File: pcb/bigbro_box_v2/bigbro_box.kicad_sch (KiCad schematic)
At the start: 41 parts, among them J1 Current Sense, J2 Display, J3 Mains, J4 UART flashing, J5 RFID, J6 Relay, K1 G5LE-1, Q1 MMBT3904, Q2 MMBT3904, Q3 BSS138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

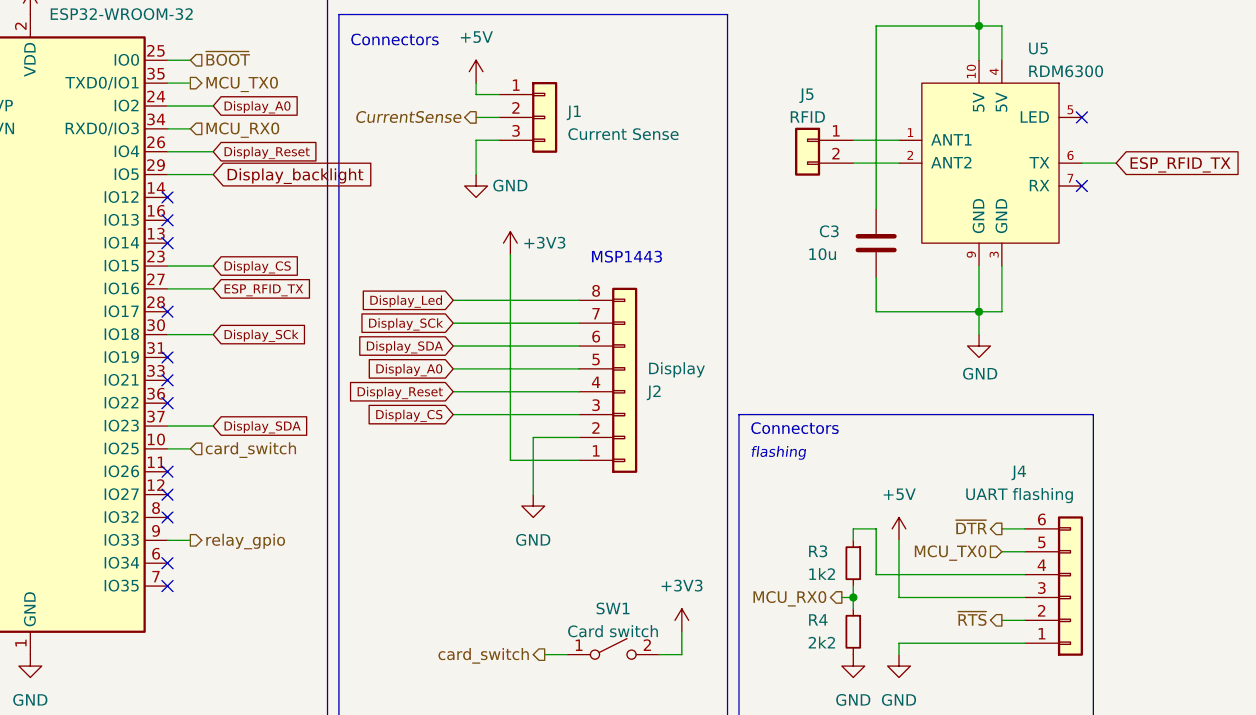
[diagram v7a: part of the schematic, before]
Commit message: Finish routing.
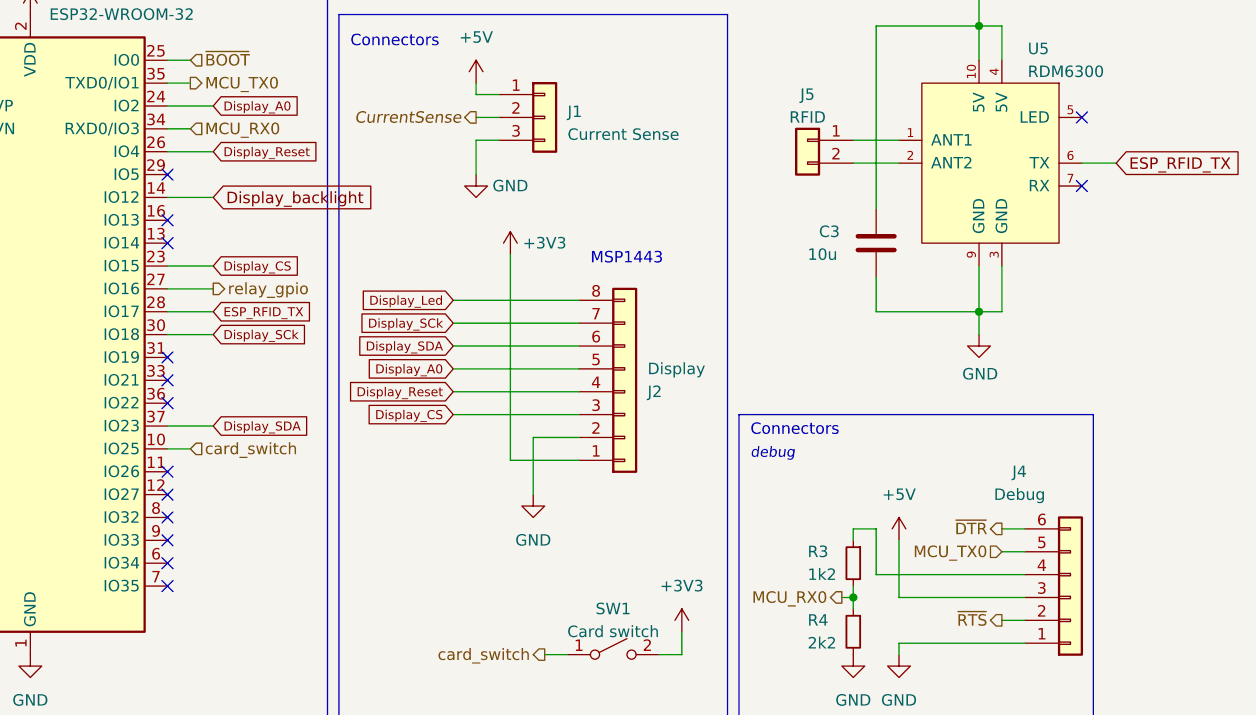
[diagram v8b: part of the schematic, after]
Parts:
- J4: value UART flashing -> Debug
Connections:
- net Display_backlight: now also U1.14 (IO12); no longer U1.29 (IO5)
- net ESP_RFID_TX: now also U1.28 (IO17); no longer U1.27 (IO16)
- net relay_gpio: now also U1.27 (IO16); no longer U1.9 (IO33)
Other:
- note added: "debug"
- note removed: "flashing"
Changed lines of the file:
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@@
   (no_connect (at 58.42 69.85))
   (no_connect (at 58.42 72.39))
+  (no_connect (at 88.9 41.91))
   (no_connect (at 58.42 34.29))
   (no_connect (at 88.9 77.47))
@@
   (no_connect (at 127 173.99))
   (no_connect (at 88.9 74.93))
-  (no_connect (at 88.9 57.15))
   (no_connect (at 88.9 62.23))
-  (no_connect (at 88.9 44.45))
+  (no_connect (at 88.9 82.55))
   (no_connect (at 154.94 173.99))
   (no_connect (at 88.9 87.63))
@@
     (stroke (width 0) (type default))
   )
-  (wire (pts (xy 88.9 82.55) (xy 91.44 82.55))
-    (stroke (width 0) (type default))
-  )
   (wire (pts (xy 149.86 147.32) (xy 149.86 148.59))
     (stroke (width 0) (type default))
@@
     (stroke (width 0) (type default))
   )
+  (wire (pts (xy 88.9 57.15) (xy 93.98 57.15))
+    (stroke (width 0) (type default))
+  )
   (wire (pts (xy 35.56 83.82) (xy 35.56 85.09))
     (stroke (width 0) (type default))
@@
     (stroke (width 0) (type default))
   )
-  (wire (pts (xy 88.9 41.91) (xy 93.98 41.91))
-    (stroke (width 0) (type default))
-  )
   (wire (pts (xy 110.49 137.16) (xy 110.49 139.7))
     (stroke (width 0) (type default))
@@
   )
   (wire (pts (xy 88.9 72.39) (xy 91.44 72.39))
+    (stroke (width 0) (type default))
+  )
+  (wire (pts (xy 88.9 44.45) (xy 93.98 44.45))
     (stroke (width 0) (type default))
   )
@@
     (effects (font (size 1.27 1.27)) (justify left bottom))
   )
-  (text "flashing" (at 153.67 73.66 0)
+  (text "debug" (at 153.67 73.66 0)
     (effects (font (size 1.15 1.15) italic) (justify left bottom))
   )
@@
     )
   )
-  (global_label "Display_backlight" (shape input) (at 93.98 41.91 0) (fields_autoplaced)
+  (global_label "Display_backlight" (shape input) (at 93.98 44.45 0) (fields_autoplaced)
     (effects (font (size 1.27 1.27)) (justify left))
-    (property "Intersheetrefs" "${INTERSHEET_REFS}" (at 112.9031 41.8306 0)
+    (property "Intersheetrefs" "${INTERSHEET_REFS}" (at 112.9031 44.3706 0)
       (effects (font (size 1.27 1.27)) (justify left) hide)
     )
   )
-  (global_label "ESP_RFID_TX" (shape input) (at 93.98 54.61 0) (fields_autoplaced)
+  (global_label "ESP_RFID_TX" (shape input) (at 93.98 57.15 0) (fields_autoplaced)
     (effects (font (size 1 1)) (justify left))
-    (property "Intersheetrefs" "${INTERSHEET_REFS}" (at 105.3086 54.5475 0)
+    (property "Intersheetrefs" "${INTERSHEET_REFS}" (at 105.3086 57.0875 0)
       (effects (font (size 1 1)) (justify left) hide)
     )
@@
     (effects (font (size 1.27 1.27)) (justify left))
   )
-  (hierarchical_label "relay_gpio" (shape output) (at 91.44 82.55 0) (fields_autoplaced)
+  (hierarchical_label "relay_gpio" (shape output) (at 93.98 54.61 0) (fields_autoplaced)
     (effects (font (size 1.27 1.27)) (justify left))
   )
@@
       (effects (font (size 1.27 1.27)))
     )
-    (property "Value" "UART flashing" (at 183.5785 77.47 0)
-      (effects (font (size 1.27 1.27)))
-    )
+    (property "Value" "Debug" (at 183.5785 77.47 0)
+      (effects (font (size 1.27 1.27)))
+    )
